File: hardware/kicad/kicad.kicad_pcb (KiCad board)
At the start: 2 copper layers, 4 parts, among them U1 RP2040

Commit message: [30-8] update progress
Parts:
- added C1: C, Capacitor_SMD:C_0603_1608Metric_Pad1.08x0.95mm_HandSolder, F.Cu at (181.0, 74.4)
- added C2: C, Capacitor_SMD:C_0603_1608Metric_Pad1.08x0.95mm_HandSolder, F.Cu at (198.3, 73.7)
- added C3: C, Capacitor_SMD:C_0603_1608Metric_Pad1.08x0.95mm_HandSolder, F.Cu at (175.5, 91.5)
- added C4: C, Capacitor_SMD:C_0603_1608Metric_Pad1.08x0.95mm_HandSolder, F.Cu at (175.4, 96.5)
- added C5: C, Capacitor_SMD:C_0603_1608Metric_Pad1.08x0.95mm_HandSolder, F.Cu at (195.6, 71.1)
- added F1: Polyfuse, Fuse:Fuse_0603_1608Metric_Pad1.05x0.95mm_HandSolder, F.Cu at (200.1, 73.7)
- added J1: Conn_01x05, Connector_PinHeader_2.54mm:PinHeader_1x05_P2.54mm_Vertical, F.Cu at (193.9, 91.7)
- added J2: USB_C_Receptacle_USB2.0, Connector_USB:USB_C_Receptacle_HRO_TYPE-C-31-M-12, F.Cu at (192.3, 62.0)
- added R4: R, Resistor_SMD:R_0603_1608Metric_Pad0.98x0.95mm_HandSolder, F.Cu at (172.3, 72.6)
- added R5: R, Resistor_SMD:R_0603_1608Metric_Pad0.98x0.95mm_HandSolder, F.Cu at (181.5, 95.2)
- added R6: R, Resistor_SMD:R_0603_1608Metric_Pad0.98x0.95mm_HandSolder, F.Cu at (195.6, 68.6)
- added R7: R, Resistor_SMD:R_0603_1608Metric_Pad0.98x0.95mm_HandSolder, F.Cu at (189.5, 69.1)
- added SW1: SW_Push, Button_Switch_SMD:SW_SPST_TL3342, F.Cu at (173.7, 66.3)
- added U2: W25Q128JVS, Package_SO:SOIC-8_5.23x5.23mm_P1.27mm, F.Cu at (178.8, 70.9)
- added U3: XC6206PxxxMR, Package_TO_SOT_SMD:SOT-23, F.Cu at (195.6, 74.1)
- added U4: USBLC6-2SC6, Package_TO_SOT_SMD:SOT-23-6, F.Cu at (190.8, 71.8)
- added Y1: Crystal_GND24_Small, Crystal:Crystal_SMD_3225-4Pin_3.2x2.5mm_HandSoldering, F.Cu at (178.1, 93.8)
- moved R1 0.92 mm to (187.8, 92.3), turned to -45 degrees
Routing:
- net VBUS: track 0.00 -> 22.3 mm
- net CS: track 1.58 -> 13.3 mm
- net +5V: track 0.00 -> 11.7 mm
- net QSPI_CLK: track 3.24 -> 14.2 mm
- net SD3: track 4.92 -> 15.8 mm
- net +3V3: track 28.8 -> 39.6 mm
- net RESET: track 2.25 -> 12.0 mm
- net SWCLK: track 3.24 -> 12.5 mm
- net Net-(R4-Pad2): track 0.00 -> 8.78 mm
- net SD1: track 1.91 -> 10.5 mm
- net SD0: track 4.98 -> 13.2 mm
- net SWD: track 4.98 -> 12.8 mm
- net D_USB_P: track 0.00 -> 7.75 mm
- net D_USB_N: track 0.00 -> 7.70 mm
- net SD2: track 2.25 -> 9.08 mm
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
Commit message: [1-9] update progress
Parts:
- added C10: C, Capacitor_SMD:C_0603_1608Metric_Pad1.08x0.95mm_HandSolder, F.Cu at (137.1, 45.6)
- added C11: C, Capacitor_SMD:C_0603_1608Metric_Pad1.08x0.95mm_HandSolder, F.Cu at (135.7, 30.5)
- added C12: C, Capacitor_SMD:C_0603_1608Metric_Pad1.08x0.95mm_HandSolder, F.Cu at (141.8, 40.4)
- added C13: C, Capacitor_SMD:C_0603_1608Metric_Pad1.08x0.95mm_HandSolder, F.Cu at (141.4, 33.2)
- added C14: C, Capacitor_SMD:C_0603_1608Metric_Pad1.08x0.95mm_HandSolder, F.Cu at (141.4, 34.9)
- added C15: C, Capacitor_SMD:C_0603_1608Metric_Pad1.08x0.95mm_HandSolder, F.Cu at (127.8, 40.6)
- added C6: C, Capacitor_SMD:C_0603_1608Metric_Pad1.08x0.95mm_HandSolder, F.Cu at (140.8, 30.5)
- added C7: C, Capacitor_SMD:C_0603_1608Metric_Pad1.08x0.95mm_HandSolder, F.Cu at (138.7, 45.0)
- added C8: C, Capacitor_SMD:C_0603_1608Metric_Pad1.08x0.95mm_HandSolder, F.Cu at (134.0, 30.5)
- added C9: C, Capacitor_SMD:C_0603_1608Metric_Pad1.08x0.95mm_HandSolder, F.Cu at (128.5, 34.2)
- moved C5 80.8 mm to (131.0, 22.7), turned to 90 degrees
- moved U3 77.4 mm to (134.5, 26.5)
- moved C2 77.2 mm to (137.2, 26.6)
- moved R7 73.3 mm to (132.8, 22.7), turned to 90 degrees
- moved F1 72.8 mm to (144.7, 26.5)
- moved C1 72.1 mm to (128.0, 25.6), turned to 0 degrees
- moved U4 68.2 mm to (139.8, 26.6), turned to 90 degrees
- moved J2 67.9 mm to (139.7, 19.1)
- moved R6 67.8 mm to (142.6, 26.4), turned to -90 degrees
- moved R3 66.8 mm to (139.1, 30.5), turned to -90 degrees
- moved U1 66.5 mm to (134.6, 38.1)
- moved R2 66.1 mm to (137.4, 30.5), turned to -90 degrees
- moved U2 65.6 mm to (128.0, 29.5), turned to 0 degrees
- moved R1 65.3 mm to (141.7, 46.0), turned to -90 degrees
- moved SW1 65.1 mm to (119.3, 30.5), turned to 90 degrees
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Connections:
- R4 pad 1: CS -> Net-(R4-Pad1)
- R4 pad 2: Net-(R4-Pad2) -> CS
- SW1 pad 2: Net-(R4-Pad2) -> Net-(R4-Pad1)
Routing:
- net GND: track 3.27 -> 34.3 mm
- net +1V1: track 7.23 -> 32.0 mm, vias 0 -> 3
- net VBUS: track 22.3 -> 11.3 mm
- net SD0: track 13.2 -> 3.95 mm
- net SD3: track 15.8 -> 6.75 mm
- net QSPI_CLK: track 14.2 -> 5.32 mm
- net Net-(R4-Pad2): track 8.78 -> 0.00 mm
- net Net-(R4-Pad1): track 0.00 -> 8.58 mm
- net unconnected-(U1-Pad36): track 5.37 -> 0.00 mm
- net unconnected-(U1-Pad8): track 5.37 -> 0.00 mm
- net unconnected-(U1-Pad35): track 5.37 -> 0.00 mm
- net unconnected-(U1-Pad7): track 5.37 -> 0.00 mm
- net unconnected-(U1-Pad39): track 4.98 -> 0.00 mm
- net unconnected-(U1-Pad11): track 4.98 -> 0.00 mm
- net unconnected-(U1-Pad37): track 4.92 -> 0.00 mm
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- added copper zone on B.Cu, net +3V3
- added copper zone on F.Cu, net GND
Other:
- board outline added: 38.1 x 44.5 mm

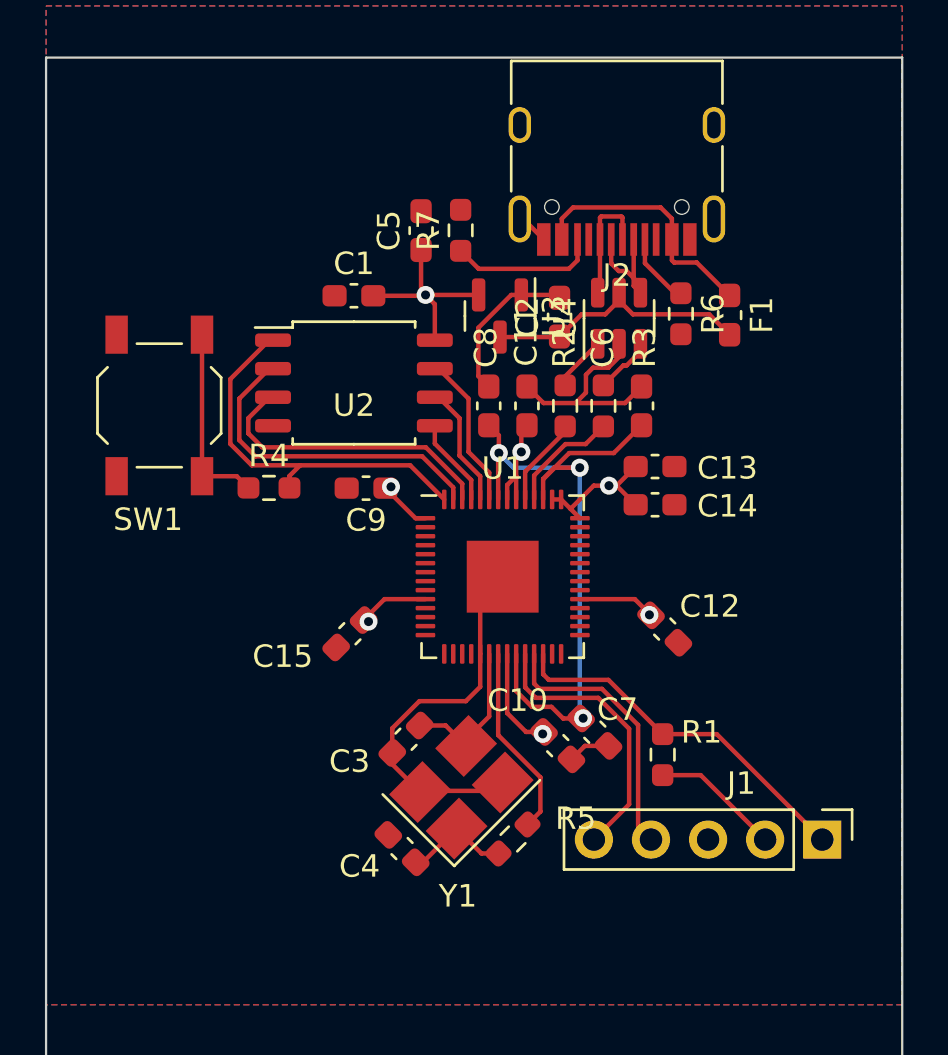
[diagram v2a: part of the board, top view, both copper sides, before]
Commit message: minor PCB changes -- RP2040+core components done (?)
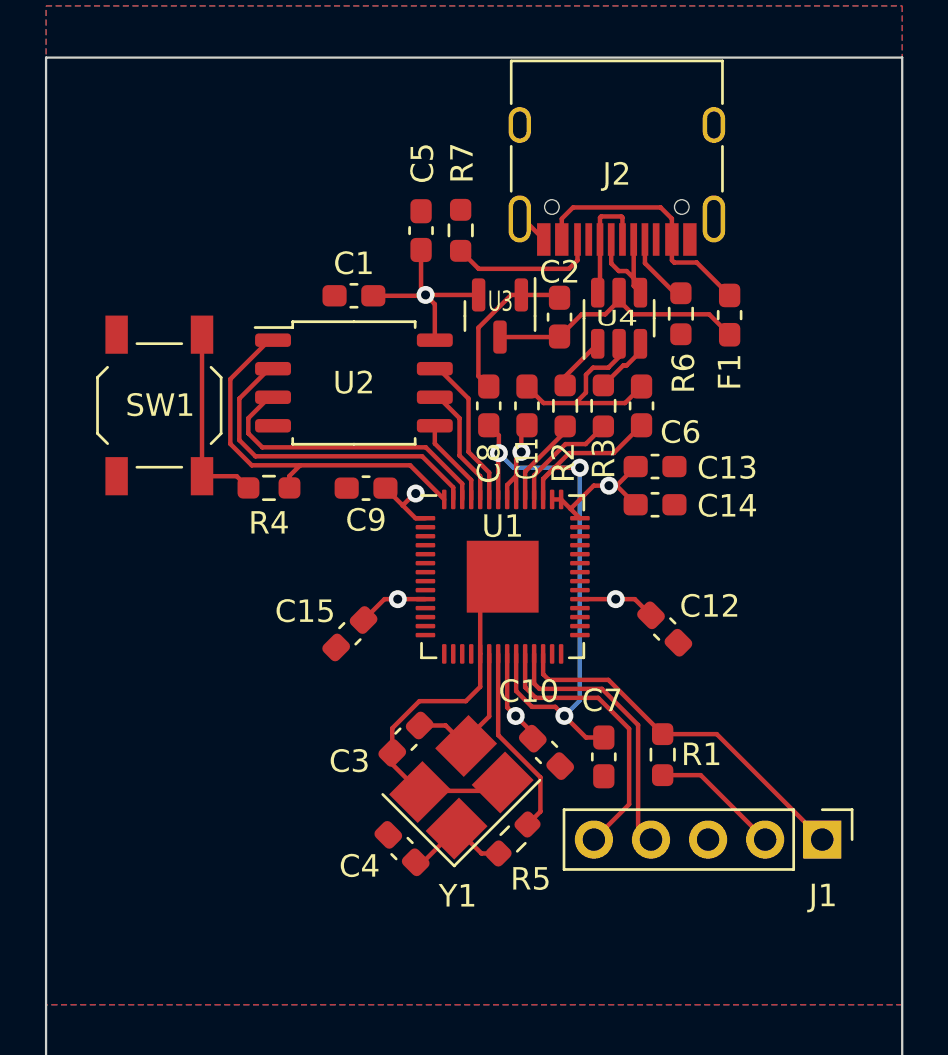
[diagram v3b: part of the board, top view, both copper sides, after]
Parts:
- moved C7 1.17 mm to (139.1, 46.1), turned to -90 degrees
- moved C10 0.58 mm to (136.6, 45.9)
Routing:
- net GND: track 34.3 -> 32.4 mm
- net +1V1: track 32.0 -> 33.2 mm

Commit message: [16-09] added level shifter + progress on the expasion connector
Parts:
- added D1: 1N4148W, Diode_SMD:D_SOD-123, B.Cu at (41.1, 70.8)
- added D10: 1N4148W, Diode_SMD:D_SOD-123, B.Cu at (60.2, 147.0)
- added D11: 1N4148W, Diode_SMD:D_SOD-123, B.Cu at (79.2, 70.8)
- added D12: 1N4148W, Diode_SMD:D_SOD-123, B.Cu at (79.2, 89.8)
- added D13: 1N4148W, Diode_SMD:D_SOD-123, B.Cu at (79.2, 108.9)
- added D14: 1N4148W, Diode_SMD:D_SOD-123, B.Cu at (79.2, 128.0)
- added D15: 1N4148W, Diode_SMD:D_SOD-123, B.Cu at (79.2, 147.0)
- added D16: 1N4148W, Diode_SMD:D_SOD-123, B.Cu at (98.3, 70.8)
- added D17: 1N4148W, Diode_SMD:D_SOD-123, B.Cu at (98.3, 89.8)
- added D18: 1N4148W, Diode_SMD:D_SOD-123, B.Cu at (98.3, 108.9)
- added D19: 1N4148W, Diode_SMD:D_SOD-123, B.Cu at (98.3, 128.0)
- added D2: 1N4148W, Diode_SMD:D_SOD-123, B.Cu at (41.1, 89.8)
- added D20: 1N4148W, Diode_SMD:D_SOD-123, B.Cu at (98.3, 147.0)
- added D21: 1N4148W, Diode_SMD:D_SOD-123, B.Cu at (117.3, 70.8)
- added D22: 1N4148W, Diode_SMD:D_SOD-123, B.Cu at (117.3, 89.8)
- added D23: 1N4148W, Diode_SMD:D_SOD-123, B.Cu at (117.3, 108.9)
- added D24: 1N4148W, Diode_SMD:D_SOD-123, B.Cu at (117.3, 128.0)
- added D25: 1N4148W, Diode_SMD:D_SOD-123, B.Cu at (117.3, 147.0)
- added D26: 1N4148W, Diode_SMD:D_SOD-123, B.Cu at (136.4, 70.8)
- added D27: 1N4148W, Diode_SMD:D_SOD-123, B.Cu at (136.4, 89.8)
- added D28: 1N4148W, Diode_SMD:D_SOD-123, B.Cu at (136.4, 108.9)
- added D29: 1N4148W, Diode_SMD:D_SOD-123, B.Cu at (136.4, 128.0)
- added D3: 1N4148W, Diode_SMD:D_SOD-123, B.Cu at (41.1, 108.9)
- added D30: 1N4148W, Diode_SMD:D_SOD-123, B.Cu at (136.4, 147.0)
- added D31: 1N4148W, Diode_SMD:D_SOD-123, B.Cu at (155.4, 70.8)
- added D32: 1N4148W, Diode_SMD:D_SOD-123, B.Cu at (155.4, 89.8)
- added D33: 1N4148W, Diode_SMD:D_SOD-123, B.Cu at (155.4, 108.9)
- added D34: 1N4148W, Diode_SMD:D_SOD-123, B.Cu at (155.4, 128.0)
- added D35: 1N4148W, Diode_SMD:D_SOD-123, B.Cu at (155.4, 147.0)
- added D4: 1N4148W, Diode_SMD:D_SOD-123, B.Cu at (41.1, 128.0)
- added D5: 1N4148W, Diode_SMD:D_SOD-123, B.Cu at (41.1, 147.0)
- added D6: 1N4148W, Diode_SMD:D_SOD-123, B.Cu at (60.2, 70.8)
- added D7: 1N4148W, Diode_SMD:D_SOD-123, B.Cu at (60.2, 89.8)
- added D8: 1N4148W, Diode_SMD:D_SOD-123, B.Cu at (60.2, 108.9)
- added D9: 1N4148W, Diode_SMD:D_SOD-123, B.Cu at (60.2, 128.0)
- added J3: Conn_01x08, Connector_PinHeader_2.54mm:PinHeader_1x08_P2.54mm_Vertical_SMD_Pin1Right, F.Cu at (188.0, 132.1)
- added LED1: MX_SK6812MINI-E, marbastlib-mx:LED_MX_6028R, B.Cu at (48.7, 73.3)
- added LED10: MX_SK6812MINI-E, marbastlib-mx:LED_MX_6028R, B.Cu at (67.8, 149.5)
- added LED11: MX_SK6812MINI-E, marbastlib-mx:LED_MX_6028R, B.Cu at (86.8, 73.3)
- added LED12: MX_SK6812MINI-E, marbastlib-mx:LED_MX_6028R, B.Cu at (86.8, 92.4)
- added LED13: MX_SK6812MINI-E, marbastlib-mx:LED_MX_6028R, B.Cu at (86.8, 111.4)
- added LED14: MX_SK6812MINI-E, marbastlib-mx:LED_MX_6028R, B.Cu at (86.8, 130.5)
- added LED15: MX_SK6812MINI-E, marbastlib-mx:LED_MX_6028R, B.Cu at (86.8, 149.5)
- added LED16: MX_SK6812MINI-E, marbastlib-mx:LED_MX_6028R, B.Cu at (105.9, 73.3)
- added LED17: MX_SK6812MINI-E, marbastlib-mx:LED_MX_6028R, B.Cu at (105.9, 92.4)
- added LED18: MX_SK6812MINI-E, marbastlib-mx:LED_MX_6028R, B.Cu at (105.9, 111.4)
- added LED19: MX_SK6812MINI-E, marbastlib-mx:LED_MX_6028R, B.Cu at (105.9, 130.5)
- added LED2: MX_SK6812MINI-E, marbastlib-mx:LED_MX_6028R, B.Cu at (48.7, 92.4)
- added LED20: MX_SK6812MINI-E, marbastlib-mx:LED_MX_6028R, B.Cu at (105.9, 149.5)
- added LED21: MX_SK6812MINI-E, marbastlib-mx:LED_MX_6028R, B.Cu at (124.9, 73.3)
- added LED22: MX_SK6812MINI-E, marbastlib-mx:LED_MX_6028R, B.Cu at (124.9, 92.4)
- added LED23: MX_SK6812MINI-E, marbastlib-mx:LED_MX_6028R, B.Cu at (124.9, 111.4)
- added LED24: MX_SK6812MINI-E, marbastlib-mx:LED_MX_6028R, B.Cu at (124.9, 130.5)
- added LED25: MX_SK6812MINI-E, marbastlib-mx:LED_MX_6028R, B.Cu at (124.9, 149.5)
- added LED26: MX_SK6812MINI-E, marbastlib-mx:LED_MX_6028R, B.Cu at (144.0, 73.3)
- added LED27: MX_SK6812MINI-E, marbastlib-mx:LED_MX_6028R, B.Cu at (144.0, 92.4)
- added LED28: MX_SK6812MINI-E, marbastlib-mx:LED_MX_6028R, B.Cu at (144.0, 111.4)
- added LED29: MX_SK6812MINI-E, marbastlib-mx:LED_MX_6028R, B.Cu at (144.0, 130.5)
- added LED3: MX_SK6812MINI-E, marbastlib-mx:LED_MX_6028R, B.Cu at (48.7, 111.4)
- added LED30: MX_SK6812MINI-E, marbastlib-mx:LED_MX_6028R, B.Cu at (144.0, 149.5)
- added LED31: MX_SK6812MINI-E, marbastlib-mx:LED_MX_6028R, B.Cu at (163.0, 73.3)
- added LED32: MX_SK6812MINI-E, marbastlib-mx:LED_MX_6028R, B.Cu at (163.0, 92.4)
- added LED33: MX_SK6812MINI-E, marbastlib-mx:LED_MX_6028R, B.Cu at (163.0, 111.4)
- added LED34: MX_SK6812MINI-E, marbastlib-mx:LED_MX_6028R, B.Cu at (163.0, 130.5)
- added LED35: MX_SK6812MINI-E, marbastlib-mx:LED_MX_6028R, B.Cu at (163.0, 149.5)
- added LED4: MX_SK6812MINI-E, marbastlib-mx:LED_MX_6028R, B.Cu at (48.7, 130.5)
- added LED5: MX_SK6812MINI-E, marbastlib-mx:LED_MX_6028R, B.Cu at (48.7, 149.5)
- added LED6: MX_SK6812MINI-E, marbastlib-mx:LED_MX_6028R, B.Cu at (67.8, 73.3)
- added LED7: MX_SK6812MINI-E, marbastlib-mx:LED_MX_6028R, B.Cu at (67.8, 92.4)
- added LED8: MX_SK6812MINI-E, marbastlib-mx:LED_MX_6028R, B.Cu at (67.8, 111.4)
- added LED9: MX_SK6812MINI-E, marbastlib-mx:LED_MX_6028R, B.Cu at (67.8, 130.5)
- added QSel3: AO3400A, Package_TO_SOT_SMD:SOT-23, B.Cu at (177.8, 124.5)
- added QSel5: AO3401A, Package_TO_SOT_SMD:SOT-23, B.Cu at (180.3, 119.4)
- added RSel1: 5k1, Resistor_SMD:R_0603_1608Metric_Pad0.98x0.95mm_HandSolder, B.Cu at (180.3, 116.8)
- added SW1: MX_SW_solder, marbastlib-mx:SW_MX_1u, F.Cu at (48.7, 68.3)
- added SW10: MX_SW_solder, marbastlib-mx:SW_MX_1u, F.Cu at (67.8, 144.5)
- added SW11: MX_SW_solder, marbastlib-mx:SW_MX_1u, F.Cu at (86.8, 68.3)
- added SW12: MX_SW_solder, marbastlib-mx:SW_MX_1u, F.Cu at (86.8, 87.3)
- added SW13: MX_SW_solder, marbastlib-mx:SW_MX_1u, F.Cu at (86.8, 106.4)
- added SW14: MX_SW_solder, marbastlib-mx:SW_MX_1u, F.Cu at (86.8, 125.4)
- added SW15: MX_SW_solder, marbastlib-mx:SW_MX_1u, F.Cu at (86.8, 144.5)
- added SW16: MX_SW_solder, marbastlib-mx:SW_MX_1u, F.Cu at (105.9, 68.3)
- added SW17: MX_SW_solder, marbastlib-mx:SW_MX_1u, F.Cu at (105.9, 87.3)
- added SW18: MX_SW_solder, marbastlib-mx:SW_MX_1u, F.Cu at (105.9, 106.4)
- added SW19: MX_SW_solder, marbastlib-mx:SW_MX_1u, F.Cu at (105.9, 125.4)
- added SW2: MX_SW_solder, marbastlib-mx:SW_MX_1u, F.Cu at (48.7, 87.3)
- added SW20: MX_SW_solder, marbastlib-mx:SW_MX_1u, F.Cu at (105.9, 144.5)
- added SW21: MX_SW_solder, marbastlib-mx:SW_MX_1u, F.Cu at (124.9, 68.3)
- added SW22: MX_SW_solder, marbastlib-mx:SW_MX_1u, F.Cu at (124.9, 87.3)
- added SW23: MX_SW_solder, marbastlib-mx:SW_MX_1u, F.Cu at (124.9, 106.4)
- added SW24: MX_SW_solder, marbastlib-mx:SW_MX_1u, F.Cu at (124.9, 125.4)
- added SW25: MX_SW_solder, marbastlib-mx:SW_MX_1u, F.Cu at (124.9, 144.5)
- added SW26: MX_SW_solder, marbastlib-mx:SW_MX_1u, F.Cu at (144.0, 68.3)
- added SW27: MX_SW_solder, marbastlib-mx:SW_MX_1u, F.Cu at (144.0, 87.3)
- added SW28: MX_SW_solder, marbastlib-mx:SW_MX_1u, F.Cu at (144.0, 106.4)
- added SW29: MX_SW_solder, marbastlib-mx:SW_MX_1u, F.Cu at (144.0, 125.4)
- added SW3: MX_SW_solder, marbastlib-mx:SW_MX_1u, F.Cu at (48.7, 106.4)
- added SW30: MX_SW_solder, marbastlib-mx:SW_MX_1u, F.Cu at (144.0, 144.5)
- added SW31: MX_SW_solder, marbastlib-mx:SW_MX_1u, F.Cu at (163.0, 68.3)
- added SW32: MX_SW_solder, marbastlib-mx:SW_MX_1u, F.Cu at (163.0, 87.3)
- added SW33: MX_SW_solder, marbastlib-mx:SW_MX_1u, F.Cu at (163.0, 106.4)
- added SW34: MX_SW_solder, marbastlib-mx:SW_MX_1u, F.Cu at (163.0, 125.4)
- added SW35: MX_SW_solder, marbastlib-mx:SW_MX_1u, F.Cu at (163.0, 144.5)
- added SW4: MX_SW_solder, marbastlib-mx:SW_MX_1u, F.Cu at (48.7, 125.4)
- added SW5: MX_SW_solder, marbastlib-mx:SW_MX_1u, F.Cu at (48.7, 144.5)
- added SW6: MX_SW_solder, marbastlib-mx:SW_MX_1u, F.Cu at (67.8, 68.3)
- added SW7: MX_SW_solder, marbastlib-mx:SW_MX_1u, F.Cu at (67.8, 87.3)
- added SW8: MX_SW_solder, marbastlib-mx:SW_MX_1u, F.Cu at (67.8, 106.4)
- added SW9: MX_SW_solder, marbastlib-mx:SW_MX_1u, F.Cu at (67.8, 125.4)
- added SWSel1: SW_DIP_x01, Button_Switch_SMD:SW_DIP_SPSTx01_Slide_6.7x4.1mm_W6.73mm_P2.54mm_LowProfile_JPin, B.Cu at (172.7, 119.4)
- added U5: 74HC595, soic:SOIC16, F.Cu at (71.1, 53.3)
- R4, R5: value R -> 1k
- R6, R7: value R -> 5k1
- moved C1 53.9 mm to (178.0, 45.6)
- moved C10 53.9 mm to (186.6, 65.9)
- moved C11 53.9 mm to (185.7, 50.5)
- moved C12 53.9 mm to (191.8, 60.4)
- moved C13 53.9 mm to (191.4, 53.2)
- moved C14 53.9 mm to (191.4, 54.9)
- moved C4 53.9 mm to (180.1, 70.2)
- moved C5 53.9 mm to (181.0, 42.7)
- moved C6 53.9 mm to (190.8, 50.5)
- moved C7 53.9 mm to (189.1, 66.1)
- moved C8 53.9 mm to (184.0, 50.5)
- moved C9 53.9 mm to (178.5, 54.2)
- moved F1 53.9 mm to (194.7, 46.5)
- moved J1 53.9 mm to (198.8, 69.8)
- moved R2 53.9 mm to (187.4, 50.5)
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- renumbered SW1 to SWR1
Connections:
- U1 pad 11: unconnected-(U1-Pad11) -> GP8
- U1 pad 12: unconnected-(U1-Pad12) -> GP9
- U1 pad 13: unconnected-(U1-Pad13) -> GP10
- U1 pad 14: unconnected-(U1-Pad14) -> GP11
- U1 pad 15: unconnected-(U1-Pad15) -> GP12
- U1 pad 16: unconnected-(U1-Pad16) -> GP13
- U1 pad 17: unconnected-(U1-Pad17) -> GP14
- U1 pad 18: unconnected-(U1-Pad18) -> GP15
- U1 pad 2: unconnected-(U1-Pad2) -> LATCH
- U1 pad 27: unconnected-(U1-Pad27) -> GP16
- U1 pad 28: unconnected-(U1-Pad28) -> GP17
- U1 pad 29: unconnected-(U1-Pad29) -> GP18
- U1 pad 3: unconnected-(U1-Pad3) -> SHIFT
- U1 pad 30: unconnected-(U1-Pad30) -> GP19
- U1 pad 31: unconnected-(U1-Pad31) -> GP20
- U1 pad 32: unconnected-(U1-Pad32) -> GP21
- U1 pad 34: unconnected-(U1-Pad34) -> GP22
- U1 pad 35: unconnected-(U1-Pad35) -> GP23
- U1 pad 36: unconnected-(U1-Pad36) -> GP24
- U1 pad 37: unconnected-(U1-Pad37) -> GP25
- U1 pad 38: unconnected-(U1-Pad38) -> ADC0
- U1 pad 39: unconnected-(U1-Pad39) -> ADC1
- U1 pad 4: unconnected-(U1-Pad4) -> COLS
- U1 pad 40: unconnected-(U1-Pad40) -> ADC2
- U1 pad 41: unconnected-(U1-Pad41) -> ADC3
- U1 pad 5: unconnected-(U1-Pad5) -> ROW0
- U1 pad 6: unconnected-(U1-Pad6) -> ROW1
- U1 pad 7: unconnected-(U1-Pad7) -> ROW2
- U1 pad 8: unconnected-(U1-Pad8) -> ROW3
- U1 pad 9: unconnected-(U1-Pad9) -> ROW4
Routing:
- net ROW4: track 0.00 -> 206.6 mm
- net ROW3: track 0.00 -> 188.7 mm
- net COL6: track 0.00 -> 186.1 mm, vias 0 -> 5
- net ROW2: track 0.00 -> 169.5 mm
- net COL5: track 0.00 -> 165.6 mm, vias 0 -> 5
- net GND: track 32.4 -> 184.9 mm, vias 0 -> 36
- net COL4: track 0.00 -> 151.3 mm, vias 0 -> 5
- net ROW1: track 0.00 -> 151.0 mm
- net ROW0: track 0.00 -> 132.4 mm
- net COL3: track 0.00 -> 132.2 mm, vias 0 -> 5
- net Net-(LED33-Pad2): track 0.00 -> 124.3 mm
- net Net-(LED3-Pad3): track 0.00 -> 124.3 mm
- net Net-(LED34-Pad2): track 0.00 -> 124.3 mm
- net Net-(LED2-Pad3): track 0.00 -> 124.3 mm
- net COL2: track 0.00 -> 116.9 mm, vias 0 -> 5
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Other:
- board size 38.1 x 44.5 mm -> 162.6 x 119.6 mm

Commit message: Update PCB
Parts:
- removed C1, C10, C11, C12, C13, C14, C15, C2, C3, C4, C5, C6, C7, C8, C9: C, Capacitor_SMD:C_0603_1608Metric_Pad1.08x0.95mm_HandSolder
- removed D1, D10, D11, D12, D13, D14, D15, D16, D17, D18, D19, D2, D20, D21, D22, D23, D24, D25, D26, D27, D28, D29, D3, D30, D31, D32, D33, D34, D35, D4, D5, D6, D7, D8, D9: 1N4148W, Diode_SMD:D_SOD-123
- removed F1: Polyfuse, Fuse:Fuse_0603_1608Metric_Pad1.05x0.95mm_HandSolder
- removed J2: USB_C_Receptacle_USB2.0, Connector_USB:USB_C_Receptacle_HRO_TYPE-C-31-M-12
- removed J3: Conn_01x08, Connector_PinHeader_2.54mm:PinHeader_1x08_P2.54mm_Vertical_SMD_Pin1Right
- removed LED32, LED33, LED34, LED35: MX_SK6812MINI-E, marbastlib-mx:LED_MX_6028R
- removed QSel3: AO3400A, Package_TO_SOT_SMD:SOT-23
- removed QSel5: AO3401A, Package_TO_SOT_SMD:SOT-23
- removed RSel1: 5k1, Resistor_SMD:R_0603_1608Metric_Pad0.98x0.95mm_HandSolder
- removed SW32, SW33, SW34, SW35: MX_SW_solder, marbastlib-mx:SW_MX_1u
- removed SWR1: SW_Push, Button_Switch_SMD:SW_SPST_TL3342
- removed SWSel1: SW_DIP_x01, Button_Switch_SMD:SW_DIP_SPSTx01_Slide_6.7x4.1mm_W6.73mm_P2.54mm_LowProfile_JPin
- removed Y1: Crystal_GND24_Small, Crystal:Crystal_SMD_3225-4Pin_3.2x2.5mm_HandSoldering
- added LED0: MX_SK6812MINI-E, marbastlib-mx:LED_MX_6028R, B.Cu at (263.0, 59.0)
- added R0: R_Small, Resistor_SMD:R_1206_3216Metric_Pad1.30x1.75mm_HandSolder, F.Cu at (278.0, 45.4)
- added R10: R_Small, Resistor_SMD:R_1206_3216Metric_Pad1.30x1.75mm_HandSolder, F.Cu at (278.0, 68.0)
- added R11: R_Small, Resistor_SMD:R_1206_3216Metric_Pad1.30x1.75mm_HandSolder, F.Cu at (299.0, 75.0)
- added R12: R_Small, Resistor_SMD:R_1206_3216Metric_Pad1.30x1.75mm_HandSolder, F.Cu at (278.0, 77.0)
- added R13: R_Small, Resistor_SMD:R_1206_3216Metric_Pad1.30x1.75mm_HandSolder, F.Cu at (278.0, 80.0)
- added R14: R_Small, Resistor_SMD:R_1206_3216Metric_Pad1.30x1.75mm_HandSolder, F.Cu at (278.0, 83.0)
- added R15: R_Small, Resistor_SMD:R_1206_3216Metric_Pad1.30x1.75mm_HandSolder, F.Cu at (278.0, 86.0)
- added R16: R_Small, Resistor_SMD:R_1206_3216Metric_Pad1.30x1.75mm_HandSolder, F.Cu at (298.0, 97.0)
- added R17: R_Small, Resistor_SMD:R_1206_3216Metric_Pad1.30x1.75mm_HandSolder, F.Cu at (278.0, 91.2)
- added R18: R_Small, Resistor_SMD:R_1206_3216Metric_Pad1.30x1.75mm_HandSolder, F.Cu at (278.0, 94.2)
- added R19: R_Small, Resistor_SMD:R_1206_3216Metric_Pad1.30x1.75mm_HandSolder, F.Cu at (278.0, 97.2)
- added R20: R_Small, Resistor_SMD:R_1206_3216Metric_Pad1.30x1.75mm_HandSolder, F.Cu at (278.0, 100.2)
- added R21: R_Small, Resistor_SMD:R_1206_3216Metric_Pad1.30x1.75mm_HandSolder, F.Cu at (278.0, 103.2)
- added R22: R_Small, Resistor_SMD:R_1206_3216Metric_Pad1.30x1.75mm_HandSolder, F.Cu at (278.0, 106.2)
- added R23: R_Small, Resistor_SMD:R_1206_3216Metric_Pad1.30x1.75mm_HandSolder, F.Cu at (278.0, 109.2)
- added R24: R_Small, Resistor_SMD:R_1206_3216Metric_Pad1.30x1.75mm_HandSolder, F.Cu at (298.0, 125.0)
- added R25: R_Small, Resistor_SMD:R_1206_3216Metric_Pad1.30x1.75mm_HandSolder, F.Cu at (278.0, 119.0)
- added R26: R_Small, Resistor_SMD:R_1206_3216Metric_Pad1.30x1.75mm_HandSolder, F.Cu at (278.0, 122.0)
- added R27: R_Small, Resistor_SMD:R_1206_3216Metric_Pad1.30x1.75mm_HandSolder, F.Cu at (278.0, 125.0)
- added R28: R_Small, Resistor_SMD:R_1206_3216Metric_Pad1.30x1.75mm_HandSolder, F.Cu at (278.0, 128.0)
- added R29: R_Small, Resistor_SMD:R_1206_3216Metric_Pad1.30x1.75mm_HandSolder, F.Cu at (278.0, 131.0)
- added R30: R_Small, Resistor_SMD:R_1206_3216Metric_Pad1.30x1.75mm_HandSolder, F.Cu at (278.0, 134.0)
- added R31: R_Small, Resistor_SMD:R_1206_3216Metric_Pad1.30x1.75mm_HandSolder, F.Cu at (278.0, 137.0)
- added R8: R_Small, Resistor_SMD:R_1206_3216Metric_Pad1.30x1.75mm_HandSolder, F.Cu at (278.0, 74.0)
- added R9: R_Small, Resistor_SMD:R_1206_3216Metric_Pad1.30x1.75mm_HandSolder, F.Cu at (278.0, 71.0)
- added SW0: MX_SW, marbastlib-mx:SW_MX_1u, B.Cu at (263.0, 54.0)
- added U6: ILI9163, my_components:ILI9163, F.Cu at (374.1, 132.4)
- added U7: ILI9341_TS, my_components:ILI9341_TS, F.Cu at (169.1, 144.2)
- added USIPO0: 74HC595, Package_SO:SO-16_3.9x9.9mm_P1.27mm, F.Cu at (337.0, 109.9)
- added USIPO1: 74HC595, Package_SO:SO-16_3.9x9.9mm_P1.27mm, F.Cu at (353.0, 109.9)
- added USIPO2: 74HC595, Package_SO:SO-16_3.9x9.9mm_P1.27mm, F.Cu at (369.0, 109.9)
- J1: value Conn_01x05 -> Conn_01x13_Female; footprint Connector_PinHeader_2.54mm:PinHeader_1x05_P2.54mm_Vertical -> Connector_PinHeader_1.00mm:PinHeader_1x13_P1.00mm_Vertical
- R1, R4, R5: value 1k -> R_Small; footprint Resistor_SMD:R_0603_1608Metric_Pad0.98x0.95mm_HandSolder -> Resistor_SMD:R_1206_3216Metric_Pad1.30x1.75mm_HandSolder
- R2, R3: value 27R -> R_Small; footprint Resistor_SMD:R_0603_1608Metric_Pad0.98x0.95mm_HandSolder -> Resistor_SMD:R_1206_3216Metric_Pad1.30x1.75mm_HandSolder
- R6, R7: value 5k1 -> R_Small; footprint Resistor_SMD:R_0603_1608Metric_Pad0.98x0.95mm_HandSolder -> Resistor_SMD:R_1206_3216Metric_Pad1.30x1.75mm_HandSolder
- SW1, SW10, SW11, SW12, SW13, SW14, SW15, SW16, SW17, SW18, SW19, SW2, SW20, SW21, SW22, SW23, SW24, SW25, SW26, SW27, SW28, SW29, SW3, SW30, SW31, SW4, SW5, SW6, SW7, SW8, SW9: value MX_SW_solder -> MX_SW; moved to B.Cu
- U1: value RP2040 -> Pico; footprint Package_DFN_QFN:QFN-56-1EP_7x7mm_P0.4mm_EP3.2x3.2mm -> MCU_RaspberryPi_and_Boards:RPi_Pico_SMD_TH
- U2: value W25Q128JVS -> MC74HC589ADR2G; footprint Package_SO:SOIC-8_5.23x5.23mm_P1.27mm -> Package_SO:SO-16_3.9x9.9mm_P1.27mm
- U3: value XC6206PxxxMR -> MC74HC589ADR2G; footprint Package_TO_SOT_SMD:SOT-23 -> Package_SO:SO-16_3.9x9.9mm_P1.27mm
- U4: value USBLC6-2SC6 -> MC74HC589ADR2G; footprint Package_TO_SOT_SMD:SOT-23-6 -> Package_SO:SO-16_3.9x9.9mm_P1.27mm
- U5: value 74HC595 -> MC74HC589ADR2G; footprint soic:SOIC16 -> Package_SO:SO-16_3.9x9.9mm_P1.27mm
- moved U5 231.3 mm to (290.0, 128.0), turned to 0 degrees
- moved U1 204.4 mm to (389.0, 54.0)
- moved LED1 195.8 mm to (244.0, 59.1)
- moved SW1 195.8 mm to (244.0, 54.0), turned to 180 degrees
- moved LED6 195.3 mm to (263.0, 78.1)
- moved SW6 195.3 mm to (263.0, 73.0), turned to 180 degrees
- moved LED2 179.4 mm to (225.0, 59.1)
- moved SW2 179.4 mm to (225.0, 54.0), turned to 180 degrees
- moved LED7 176.8 mm to (244.0, 78.1)
- moved SW7 176.8 mm to (244.0, 73.0), turned to 180 degrees
- moved LED12 176.2 mm to (263.0, 97.1)
- moved SW12 176.2 mm to (263.0, 92.0), turned to 180 degrees
- moved LED31 168.7 mm to (278.8, 196.1)
- moved SW31 168.7 mm to (278.8, 191.0), turned to 180 degrees
- moved LED3 165.8 mm to (206.0, 59.1)
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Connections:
- J1 pad 1: RESET -> +3V3
- J1 pad 2: +3V3 -> unconnected-(J1-Pad2)
- J1 pad 4: SWD -> SCK
- J1 pad 5: SWCLK -> unconnected-(J1-Pad5)
- LED1 pad 3: WS2812 -> Net-(LED0-Pad2)
- LED11 pad 3: Net-(LED11-Pad3) -> Net-(LED10-Pad2)
- LED12 pad 3: Net-(LED12-Pad3) -> Net-(LED11-Pad2)
- LED13 pad 3: Net-(LED13-Pad3) -> Net-(LED12-Pad2)
- LED14 pad 3: Net-(LED14-Pad3) -> Net-(LED13-Pad2)
- LED15 pad 3: Net-(LED10-Pad2) -> Net-(LED14-Pad2)
- LED16 pad 3: Net-(LED11-Pad2) -> Net-(LED15-Pad2)
- LED17 pad 3: Net-(LED12-Pad2) -> Net-(LED16-Pad2)
- LED18 pad 3: Net-(LED13-Pad2) -> Net-(LED17-Pad2)
- LED19 pad 3: Net-(LED14-Pad2) -> Net-(LED18-Pad2)
- LED2 pad 3: Net-(LED2-Pad3) -> Net-(LED1-Pad2)
- LED20 pad 3: Net-(LED15-Pad2) -> Net-(LED19-Pad2)
- LED21 pad 3: Net-(LED16-Pad2) -> Net-(LED20-Pad2)
- LED22 pad 3: Net-(LED17-Pad2) -> Net-(LED21-Pad2)
- LED23 pad 3: Net-(LED18-Pad2) -> Net-(LED22-Pad2)
- LED24 pad 3: Net-(LED19-Pad2) -> Net-(LED23-Pad2)
- LED25 pad 3: Net-(LED20-Pad2) -> Net-(LED24-Pad2)
- LED26 pad 3: Net-(LED21-Pad2) -> Net-(LED25-Pad2)
- LED27 pad 3: Net-(LED22-Pad2) -> Net-(LED26-Pad2)
- LED28 pad 3: Net-(LED23-Pad2) -> Net-(LED27-Pad2)
- LED29 pad 3: Net-(LED24-Pad2) -> Net-(LED28-Pad2)
- LED3 pad 3: Net-(LED3-Pad3) -> Net-(LED2-Pad2)
- LED30 pad 3: Net-(LED25-Pad2) -> Net-(LED29-Pad2)
- LED31 pad 2: Net-(LED2-Pad3) -> unconnected-(LED31-Pad2)
- LED31 pad 3: Net-(LED26-Pad2) -> Net-(LED30-Pad2)
- LED4 pad 3: Net-(LED33-Pad2) -> Net-(LED3-Pad2)
- LED5 pad 2: Net-(LED10-Pad3) -> Net-(LED5-Pad2)
- LED5 pad 3: Net-(LED34-Pad2) -> Net-(LED4-Pad2)
- LED6 pad 2: Net-(LED11-Pad3) -> Net-(LED6-Pad2)
- LED6 pad 3: Net-(LED1-Pad2) -> Net-(LED5-Pad2)
- LED7 pad 2: Net-(LED12-Pad3) -> Net-(LED7-Pad2)
- LED7 pad 3: Net-(LED2-Pad2) -> Net-(LED6-Pad2)
- LED8 pad 2: Net-(LED13-Pad3) -> Net-(LED8-Pad2)
- LED8 pad 3: Net-(LED3-Pad2) -> Net-(LED7-Pad2)
- LED9 pad 2: Net-(LED14-Pad3) -> Net-(LED10-Pad3)
- LED9 pad 3: Net-(LED4-Pad2) -> Net-(LED8-Pad2)
- R1 pad 1: RESET -> GND
- R1 pad 2: +3V3 -> Net-(R1-Pad2)
- R2 pad 1: D_P -> GND
- R3 pad 1: D_N -> GND
- R4 pad 1: Net-(R4-Pad1) -> GND
- R4 pad 2: CS -> Net-(R4-Pad2)
- R5 pad 1: Net-(C4-Pad2) -> GND
- R5 pad 2: XTAL_OUT -> Net-(R5-Pad2)
- R6 pad 1: Net-(J2-PadA5) -> GND
- R6 pad 2: GND -> Net-(R6-Pad2)
- R7 pad 1: Net-(J2-PadB5) -> GND
- R7 pad 2: GND -> Net-(R7-Pad2)
- SW1 pad 1: Net-(D1-Pad2) -> +3V3
- SW1 pad 2: ROW0 -> Net-(R1-Pad2)
- SW10 pad 1: Net-(D10-Pad2) -> +3V3
- SW10 pad 2: ROW4 -> Net-(R10-Pad2)
- SW11 pad 1: Net-(D11-Pad2) -> +3V3
- SW11 pad 2: ROW0 -> Net-(R11-Pad2)
- SW12 pad 1: Net-(D12-Pad2) -> +3V3
- SW12 pad 2: ROW1 -> Net-(R12-Pad2)
- SW13 pad 1: Net-(D13-Pad2) -> +3V3
- SW13 pad 2: ROW2 -> Net-(R13-Pad2)
- SW14 pad 1: Net-(D14-Pad2) -> +3V3
- SW14 pad 2: ROW3 -> Net-(R14-Pad2)
- SW15 pad 1: Net-(D15-Pad2) -> +3V3
- SW15 pad 2: ROW4 -> Net-(R15-Pad2)
- SW16 pad 1: Net-(D16-Pad2) -> +3V3
- SW16 pad 2: ROW0 -> Net-(R16-Pad2)
- SW17 pad 1: Net-(D17-Pad2) -> +3V3
- SW17 pad 2: ROW1 -> Net-(R17-Pad2)
- SW18 pad 1: Net-(D18-Pad2) -> +3V3
- SW18 pad 2: ROW2 -> Net-(R18-Pad2)
- SW19 pad 1: Net-(D19-Pad2) -> +3V3
- SW19 pad 2: ROW3 -> Net-(R19-Pad2)
- SW2 pad 1: Net-(D2-Pad2) -> +3V3
- SW2 pad 2: ROW1 -> Net-(R2-Pad2)
- SW20 pad 1: Net-(D20-Pad2) -> +3V3
- SW20 pad 2: ROW4 -> Net-(R20-Pad2)
- SW21 pad 1: Net-(D21-Pad2) -> +3V3
- SW21 pad 2: ROW0 -> Net-(R21-Pad2)
- SW22 pad 1: Net-(D22-Pad2) -> +3V3
- SW22 pad 2: ROW1 -> Net-(R22-Pad2)
- SW23 pad 1: Net-(D23-Pad2) -> +3V3
- SW23 pad 2: ROW2 -> Net-(R23-Pad2)
- SW24 pad 1: Net-(D24-Pad2) -> +3V3
- SW24 pad 2: ROW3 -> Net-(R24-Pad2)
- SW25 pad 1: Net-(D25-Pad2) -> +3V3
- SW25 pad 2: ROW4 -> Net-(R25-Pad2)
- SW26 pad 1: Net-(D26-Pad2) -> +3V3
- SW26 pad 2: ROW0 -> Net-(R26-Pad2)
- SW27 pad 1: Net-(D27-Pad2) -> +3V3
- SW27 pad 2: ROW1 -> Net-(R27-Pad2)
- SW28 pad 1: Net-(D28-Pad2) -> +3V3
- SW28 pad 2: ROW2 -> Net-(R28-Pad2)
- SW29 pad 1: Net-(D29-Pad2) -> +3V3
- SW29 pad 2: ROW3 -> Net-(R29-Pad2)
- SW3 pad 1: Net-(D3-Pad2) -> +3V3
- SW3 pad 2: ROW2 -> Net-(R3-Pad2)
- SW30 pad 1: Net-(D30-Pad2) -> +3V3
- SW30 pad 2: ROW4 -> Net-(R30-Pad2)
- SW31 pad 1: Net-(D31-Pad2) -> +3V3
- SW31 pad 2: ROW0 -> Net-(R31-Pad2)
- SW4 pad 1: Net-(D4-Pad2) -> +3V3
- SW4 pad 2: ROW3 -> Net-(R4-Pad2)
- SW5 pad 1: Net-(D5-Pad2) -> +3V3
- SW5 pad 2: ROW4 -> Net-(R5-Pad2)
- SW6 pad 1: Net-(D6-Pad2) -> +3V3
- SW6 pad 2: ROW0 -> Net-(R6-Pad2)
- SW7 pad 1: Net-(D7-Pad2) -> +3V3
- SW7 pad 2: ROW1 -> Net-(R7-Pad2)
- SW8 pad 1: Net-(D8-Pad2) -> +3V3
- SW8 pad 2: ROW2 -> Net-(R8-Pad2)
- SW9 pad 1: Net-(D9-Pad2) -> +3V3
- SW9 pad 2: ROW3 -> Net-(R9-Pad2)
- U1 pad 1: +3V3 -> RGB_DATA
- U1 pad 10: +3V3 -> unconnected-(U1-Pad10)
- U1 pad 11: GP8 -> unconnected-(U1-Pad11)
- U1 pad 12: GP9 -> unconnected-(U1-Pad12)
- U1 pad 13: GP10 -> GND
- U1 pad 14: GP11 -> REGISTER_SCK
- U1 pad 15: GP12 -> REGISTER_MOSI
- U1 pad 16: GP13 -> REGISTER_MISO
- U1 pad 17: GP14 -> SIPO_CS
- U1 pad 18: GP15 -> GND
- U1 pad 19: GND -> PISO_CS
- U1 pad 2: LATCH -> unconnected-(U1-Pad2)
- U1 pad 20: XTAL_IN -> PISO_LATCH
- U1 pad 21: XTAL_OUT -> unconnected-(U1-Pad21)
- U1 pad 22: +3V3 -> unconnected-(U1-Pad22)
- U1 pad 23: +1V1 -> GND
- U1 pad 24: SWCLK -> unconnected-(U1-Pad24)
- U1 pad 25: SWD -> unconnected-(U1-Pad25)
- U1 pad 26: RESET -> unconnected-(U1-Pad26)
- U1 pad 27: GP16 -> unconnected-(U1-Pad27)
- U1 pad 28: GP17 -> GND
- U1 pad 29: GP18 -> unconnected-(U1-Pad29)
- U1 pad 3: SHIFT -> GND
- U1 pad 30: GP19 -> unconnected-(U1-Pad30)
- U1 pad 31: GP20 -> unconnected-(U1-Pad31)
- U1 pad 32: GP21 -> unconnected-(U1-Pad32)
- U1 pad 33: +3V3 -> unconnected-(U1-Pad33)
- U1 pad 34: GP22 -> unconnected-(U1-Pad34)
- U1 pad 35: GP23 -> unconnected-(U1-Pad35)
- U1 pad 36: GP24 -> +3V3
- U1 pad 37: GP25 -> unconnected-(U1-Pad37)
- U1 pad 38: ADC0 -> GND
- U1 pad 39: ADC1 -> unconnected-(U1-Pad39)
- U1 pad 4: COLS -> SCK
- U1 pad 40: ADC2 -> unconnected-(U1-Pad40)
- U1 pad 41: ADC3 -> unconnected-(U1-Pad41)
- U1 pad 42: +3V3 -> unconnected-(U1-Pad42)
- U1 pad 43: +3V3 -> unconnected-(U1-Pad43)
- U1 pad 5: ROW0 -> MOSI
- U1 pad 6: ROW1 -> MISO
- U1 pad 7: ROW2 -> unconnected-(U1-Pad7)
- U1 pad 8: ROW3 -> GND
- U1 pad 9: ROW4 -> unconnected-(U1-Pad9)
- U2 pad 1: CS -> Net-(R0-Pad2)
- U2 pad 2: SD1 -> Net-(R1-Pad2)
- U2 pad 3: SD2 -> Net-(R2-Pad2)
- U2 pad 4: GND -> Net-(R3-Pad2)
- U2 pad 5: SD0 -> Net-(R4-Pad2)
- U2 pad 6: QSPI_CLK -> Net-(R5-Pad2)
- U2 pad 7: SD3 -> Net-(R7-Pad2)
- U2 pad 8: +3V3 -> GND
- U3 pad 1: GND -> Net-(R10-Pad2)
- U3 pad 2: +3V3 -> Net-(R9-Pad2)
- U3 pad 3: +5V -> Net-(R8-Pad2)
- U4 pad 1: D_P -> Net-(R16-Pad2)
- U4 pad 2: GND -> Net-(R17-Pad2)
- U4 pad 3: D_N -> Net-(R18-Pad2)
- U4 pad 4: D_USB_N -> Net-(R19-Pad2)
- U4 pad 5: +5V -> Net-(R20-Pad2)
- U4 pad 6: D_USB_P -> Net-(R21-Pad2)
- U5 pad 1: COL0 -> Net-(R24-Pad2)
- U5 pad 10: GND -> PISO_CS
- U5 pad 11: SHIFT -> REGISTER_SCK
- U5 pad 12: LATCH -> PISO_LATCH
- U5 pad 13: GND -> unconnected-(U5-Pad13)
- U5 pad 15: unconnected-(U5-Pad15) -> Net-(R31-Pad2)
- U5 pad 2: COL1 -> Net-(R25-Pad2)
- U5 pad 3: COL2 -> Net-(R26-Pad2)
- U5 pad 4: COL3 -> Net-(R27-Pad2)
- U5 pad 5: COL4 -> Net-(R28-Pad2)
- U5 pad 6: COL5 -> Net-(R29-Pad2)
- U5 pad 7: COL6 -> Net-(R30-Pad2)
- U5 pad 9: COLS -> Net-(U4-Pad14)
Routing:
- net ROW4: track 206.6 -> 0.00 mm
- net ROW3: track 188.7 -> 0.00 mm
- net COL6: track 186.1 -> 0.00 mm, vias 5 -> 0
- net GND: track 184.9 -> 0.00 mm, vias 36 -> 0
- net ROW2: track 169.5 -> 0.00 mm
- net COL5: track 165.6 -> 0.00 mm, vias 5 -> 0
- net COL4: track 151.3 -> 0.00 mm, vias 5 -> 0
- net ROW1: track 151.0 -> 0.00 mm
- net Net-(R11-Pad2): track 0.00 -> 143.3 mm, vias 0 -> 1
- net Net-(R5-Pad2): track 0.00 -> 142.5 mm, vias 0 -> 1
- net ROW0: track 132.4 -> 0.00 mm
- net COL3: track 132.2 -> 0.00 mm, vias 5 -> 0
- net Net-(LED33-Pad2): track 124.3 -> 0.00 mm
- net Net-(LED3-Pad3): track 124.3 -> 0.00 mm
- net Net-(LED34-Pad2): track 124.3 -> 0.00 mm
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- removed copper zone on B.Cu, net +3V3
- removed copper zone on F.Cu, net GND
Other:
- board size 162.6 x 119.6 mm -> 272 x 197 mm
